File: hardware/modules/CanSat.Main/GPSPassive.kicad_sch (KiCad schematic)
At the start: 14 parts, among them J103 SMA, U104 NEO-M9N-00B

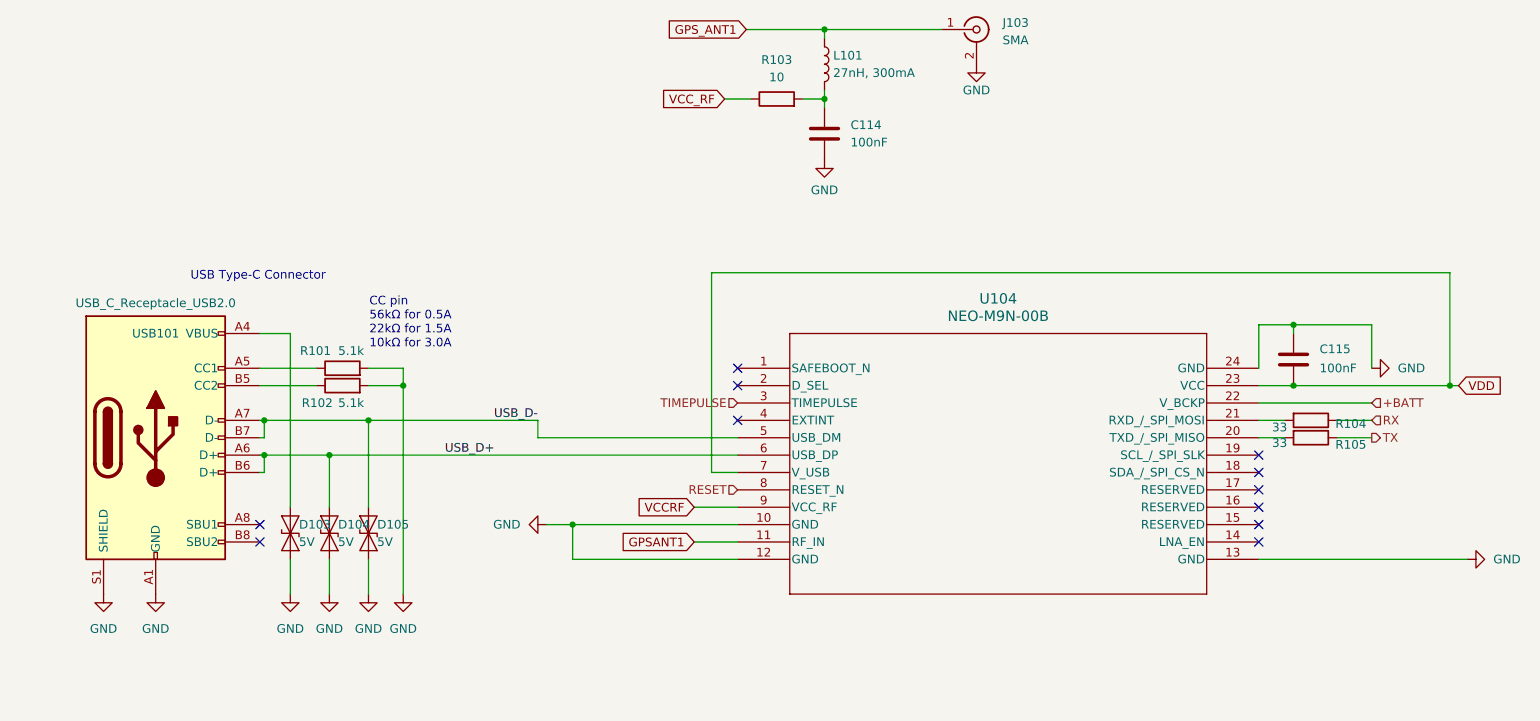
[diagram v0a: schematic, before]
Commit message: GPSActiveをGPSPassiveに変更
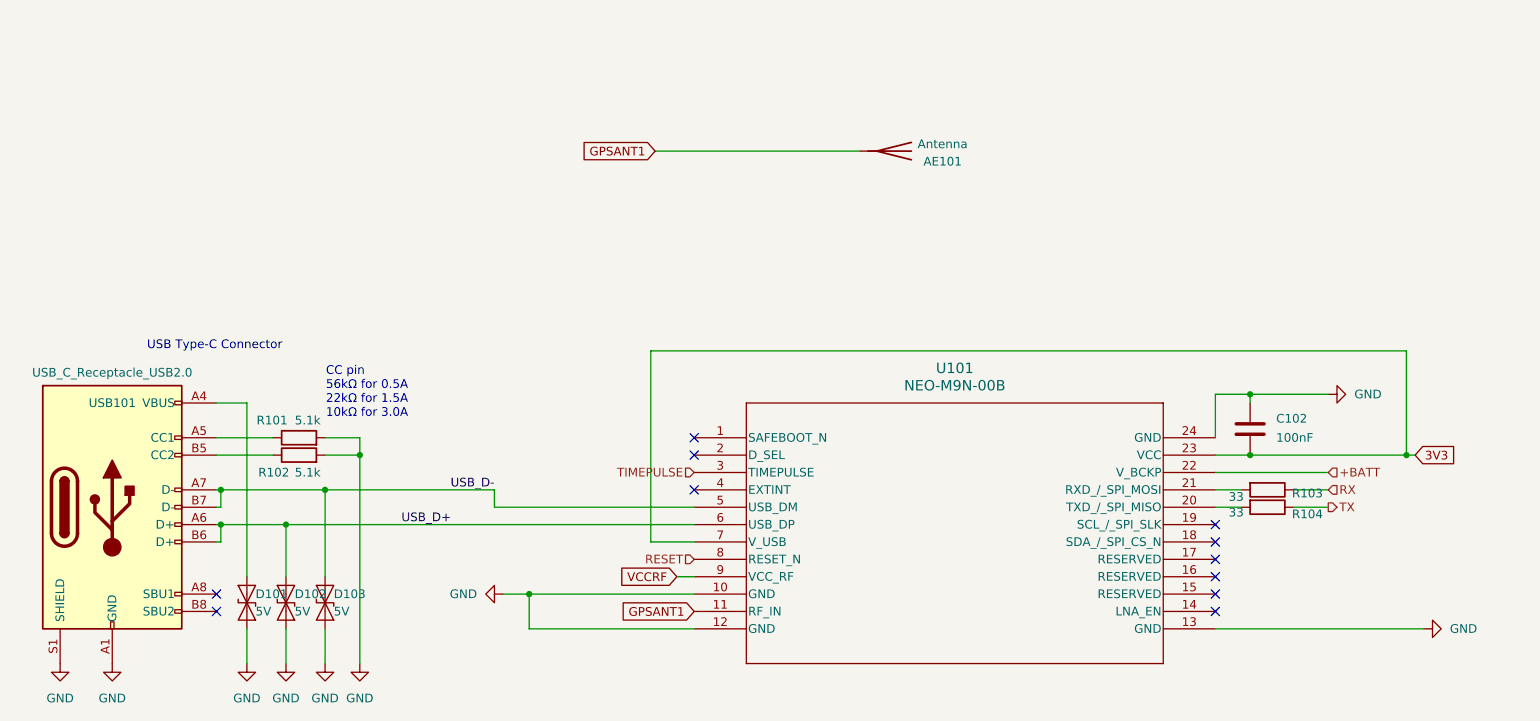
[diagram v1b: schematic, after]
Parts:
- removed C114, C115: 100nF, Capacitor_SMD:C_0402_1005Metric, symbol Device:C
- removed D104, D105: 5V, Diode_SMD:D_SOD-882D, symbol Diode:ESD9B5.0ST5G
- removed J103: SMA, Connector_Coaxial:SMA_Amphenol_132203-12_Horizontal, symbol Connector:Conn_Coaxial
- removed L101: 27nH, 300mA, Inductor_SMD:L_0402_1005Metric, symbol Device:L
- removed R105: 33, Resistor_SMD:R_0402_1005Metric, symbol Device:R
- removed U104: NEO-M9N-00B, WOBClibrary:SMT_9N-00B_UBL, symbol WOBClibrary:NEO-M9N-00B
- added AE101: Antenna, WOBClibrary:GNSS_Antenna_1212, symbol Device:Antenna
- added C102: 100nF, Capacitor_SMD:C_0402_1005Metric, symbol Device:C
- added D101, D102: 5V, Diode_SMD:D_SOD-882D, symbol Diode:ESD9B5.0ST5G
- added U101: NEO-M9N-00B, WOBCLibrary:ATGM332D-5N31, symbol WOBClibrary:NEO-M9N-00B
- R103: value 10 -> 33; LCSC C25077 -> C25105
- USB101: footprint WOBCLibrary:USB_C_TYPEC-301S-ACP16X7 -> Connector_USB:USB_C_Receptacle_XKB_U262-16XN-4BVC11
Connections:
- net VCC_RF is gone; now on net RX: R103.1
- net +BATT: now also U101.22 (V_BCKP)
- net GND: now also C102.1, D101.1 (A1), D102.1 (A1), U101.10 (GND), U101.12 (GND), U101.13 (GND), U101.24 (GND)
- net GPSANT1: now also AE101.1 (A), U101.11 (RF_IN)
- net RESET: now also U101.8 (RESET_N)
- net RX: no longer R104.1
- net TIMEPULSE: now also U101.3 (TIMEPULSE)
- net TX: now also R104.1
- net USB_D+: now also D102.2 (A2), U101.6 (USB_DP)
- net USB_D-: now also D103.2 (A2), U101.5 (USB_DM)
- net VCCRF: now also U101.9 (VCC_RF)
- net at R103.2: now also U101.21 (RXD_/_SPI_MOSI)
- net at USB101.A4 (VBUS), USB101.A9 (VBUS), USB101.B4 (VBUS)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: now also D101.2 (A2); no longer D103.2 (A2)
- net at R104.2: now also U101.20 (TXD_/_SPI_MISO)
- new net 3V3: C102.2, U101.23 (VCC), U101.7 (V_USB)

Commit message: 2/3配置
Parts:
- AE101: footprint WOBClibrary:GNSS_Antenna_1212 -> WOBCLibrary:GNSS_Antenna_1212
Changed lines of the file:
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@@
 			(project "GPSPassive"
 				(path "/bbee8c47-266c-4026-940d-10a37b262ebb/4b90791a-8d7f-4620-926a-57dc74f8fc96"
-					(reference "#PWR0105")
+					(reference "#PWR0705")
 					(unit 1)
 				)
@@
 			(project "GPSPassive"
 				(path "/bbee8c47-266c-4026-940d-10a37b262ebb/4b90791a-8d7f-4620-926a-57dc74f8fc96"
-					(reference "#PWR0102")
+					(reference "#PWR0702")
 					(unit 1)
 				)
@@
 			(project "GPSPassive"
 				(path "/bbee8c47-266c-4026-940d-10a37b262ebb/4b90791a-8d7f-4620-926a-57dc74f8fc96"
-					(reference "D102")
+					(reference "D702")
 					(unit 1)
 				)
@@
 			(project "GPSPassive"
 				(path "/bbee8c47-266c-4026-940d-10a37b262ebb/4b90791a-8d7f-4620-926a-57dc74f8fc96"
-					(reference "USB101")
+					(reference "USB701")
 					(unit 1)
 				)
@@
 			(project "GPSPassive"
 				(path "/bbee8c47-266c-4026-940d-10a37b262ebb/4b90791a-8d7f-4620-926a-57dc74f8fc96"
-					(reference "#PWR0110")
+					(reference "#PWR0709")
 					(unit 1)
 				)
@@
 			(project "GPSPassive"
 				(path "/bbee8c47-266c-4026-940d-10a37b262ebb/4b90791a-8d7f-4620-926a-57dc74f8fc96"
-					(reference "#PWR0107")
+					(reference "#PWR0707")
 					(unit 1)
 				)
@@
 			(project "GPSPassive"
 				(path "/bbee8c47-266c-4026-940d-10a37b262ebb/4b90791a-8d7f-4620-926a-57dc74f8fc96"
-					(reference "#PWR0108")
+					(reference "#PWR0708")
 					(unit 1)
 				)
@@
 			(project "GPSPassive"
 				(path "/bbee8c47-266c-4026-940d-10a37b262ebb/4b90791a-8d7f-4620-926a-57dc74f8fc96"
-					(reference "R102")
+					(reference "R702")
 					(unit 1)
 				)
@@
 			(project "GPSPassive"
 				(path "/bbee8c47-266c-4026-940d-10a37b262ebb/4b90791a-8d7f-4620-926a-57dc74f8fc96"
-					(reference "R104")
+					(reference "R704")
 					(unit 1)
 				)
@@
 			(project "GPSPassive"
 				(path "/bbee8c47-266c-4026-940d-10a37b262ebb/4b90791a-8d7f-4620-926a-57dc74f8fc96"
-					(reference "#PWR0106")
+					(reference "#PWR0706")
 					(unit 1)
 				)
@@
 			(project "GPSPassive"
 				(path "/bbee8c47-266c-4026-940d-10a37b262ebb/4b90791a-8d7f-4620-926a-57dc74f8fc96"
-					(reference "#PWR0103")
+					(reference "#PWR0703")
 					(unit 1)
 				)
@@
 			)
 		)
-		(property "Footprint" "WOBClibrary:GNSS_Antenna_1212"
+		(property "Footprint" "WOBCLibrary:GNSS_Antenna_1212"
 			(at 172.72 64.77 0)
 			(effects
@@
 			(project "GPSPassive"
 				(path "/bbee8c47-266c-4026-940d-10a37b262ebb/4b90791a-8d7f-4620-926a-57dc74f8fc96"
-					(reference "AE101")
+					(reference "AE701")
 					(unit 1)
 				)
@@
 			(project "GPSPassive"
 				(path "/bbee8c47-266c-4026-940d-10a37b262ebb/4b90791a-8d7f-4620-926a-57dc74f8fc96"
-					(reference "#PWR0101")
+					(reference "#PWR0701")
 					(unit 1)
 				)
@@
 			(project "GPSPassive"
 				(path "/bbee8c47-266c-4026-940d-10a37b262ebb/4b90791a-8d7f-4620-926a-57dc74f8fc96"
-					(reference "D101")
+					(reference "D701")
 					(unit 1)
 				)
@@
 			(project "GPSPassive"
 				(path "/bbee8c47-266c-4026-940d-10a37b262ebb/4b90791a-8d7f-4620-926a-57dc74f8fc96"
-					(reference "C102")
+					(reference "C701")
 					(unit 1)
 				)
@@
 			(project "GPSPassive"
 				(path "/bbee8c47-266c-4026-940d-10a37b262ebb/4b90791a-8d7f-4620-926a-57dc74f8fc96"
-					(reference "U101")
+					(reference "U701")
 					(unit 1)
 				)
@@
 			(project "GPSPassive"
 				(path "/bbee8c47-266c-4026-940d-10a37b262ebb/4b90791a-8d7f-4620-926a-57dc74f8fc96"
-					(reference "R101")
+					(reference "R701")
 					(unit 1)
 				)
@@
 			(project "GPSPassive"
 				(path "/bbee8c47-266c-4026-940d-10a37b262ebb/4b90791a-8d7f-4620-926a-57dc74f8fc96"
-					(reference "#PWR0104")
+					(reference "#PWR0704")
 					(unit 1)
 				)
@@
 			(project "GPSPassive"
 				(path "/bbee8c47-266c-4026-940d-10a37b262ebb/4b90791a-8d7f-4620-926a-57dc74f8fc96"
-					(reference "D103")
+					(reference "D703")
 					(unit 1)
 				)
@@
 			(project "GPSPassive"
 				(path "/bbee8c47-266c-4026-940d-10a37b262ebb/4b90791a-8d7f-4620-926a-57dc74f8fc96"
-					(reference "R103")
-					(unit 1)
-				)
+					(reference "R703")
+					(unit 1)
+				)

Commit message: とりあえず配置完了
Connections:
- net 3V3 renamed VDD
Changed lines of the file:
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@@
 	(wire
 		(pts
-			(xy 247.65 109.22) (xy 248.92 109.22)
+			(xy 247.65 109.22) (xy 255.27 109.22)
 		)
 		(stroke
@@
 		(pts
 			(xy 83.82 119.38) (xy 83.82 127)
+		)
+		(stroke
+			(width 0)
+			(type default)
+		)
+	)
+	(wire
+		(pts
+			(xy 255.27 106.045) (xy 255.27 109.22)
 		)
 		(stroke
@@
 				)
 				(justify right)
-				(hide yes)
-			)
-		)
-	)
-	(global_label "3V3"
-		(shape input)
-		(at 248.92 109.22 0)
-		(fields_autoplaced yes)
-		(effects
-			(font
-				(size 1.27 1.27)
-			)
-			(justify left)
-		)
-		(property "Intersheetrefs" "${INTERSHEET_REFS}"
-			(at 255.4128 109.22 0)
-			(effects
-				(font
-					(size 1.27 1.27)
-				)
-				(justify left)
 				(hide yes)
 			)
@@
 					(unit 1)
 				)
+			)
+		)
+	)
+	(symbol
+		(lib_id "power:VDD")
+		(at 255.27 106.045 0)
+		(unit 1)
+		(exclude_from_sim no)
+		(in_bom yes)
+		(on_board yes)
+		(dnp no)
+		(fields_autoplaced yes)
+		(property "Reference" "#PWR0710"
+			(at 255.27 109.855 0)
+			(effects
+				(font
+					(size 1.27 1.27)
+				)
+				(hide yes)
+			)
+		)
+		(property "Value" "VDD"
+			(at 255.27 101.6 0)
+			(effects
+				(font
+					(size 1.27 1.27)
+				)
+			)
+		)
+		(property "Footprint" ""
+			(at 255.27 106.045 0)
+			(effects
+				(font
+					(size 1.27 1.27)
+				)
+				(hide yes)
+			)
+		)
+		(property "Datasheet" ""
+			(at 255.27 106.045 0)
+			(effects
+				(font
+					(size 1.27 1.27)
+				)
+				(hide yes)
+			)
+		)
+		(property "Description" "Power symbol creates a global label with name \"VDD\""
+			(at 255.27 106.045 0)
+			(effects
+				(font
+					(size 1.27 1.27)
+				)
+				(hide yes)
+			)
+		)
+		(pin "1"
+		)
+		(instances
+			(project ""
+				(path "/bbee8c47-266c-4026-940d-10a37b262ebb/4b90791a-8d7f-4620-926a-57dc74f8fc96"
+					(reference "#PWR0710")
+					(unit 1)
+				)

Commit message: ガーバーファイル出力
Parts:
- USB101: footprint Connector_USB:USB_C_Receptacle_XKB_U262-16XN-4BVC11 -> WOBCLibrary:USB_C_TYPEC-301S-ACP16X7; LCSC C2982481 -> C2856766
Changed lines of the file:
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@@
 			)
 		)
-		(property "Footprint" "Connector_USB:USB_C_Receptacle_XKB_U262-16XN-4BVC11"
+		(property "Footprint" "WOBCLibrary:USB_C_TYPEC-301S-ACP16X7"
 			(at 62.23 116.84 0)
 			(effects
@@
 			)
 		)
-		(property "LCSC" "C2982481"
+		(property "LCSC" "C2856766"
 			(at 58.42 116.84 0)
 			(effects
